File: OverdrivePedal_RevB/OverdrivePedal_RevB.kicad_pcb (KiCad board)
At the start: 2 copper layers, 26.7 x 33.7 mm, 23 parts, among them J1 Conn_01x02, J2 Conn_01x02, J3 Conn_01x03, J4 Conn_01x03, J5 Conn_01x03, J6 Conn_01x02, U1 TL072, U2 NCP1729, U3 MIC5233-5.0YM5-TR, U4 MIC5270-5.0YM5-TR

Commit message: modified RevB
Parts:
- removed U1: TL072, Package_SO:TSSOP-8_4.4x3mm_P0.65mm
- added C10: 330nF, Capacitor_SMD:C_0805_2012Metric_Pad1.15x1.40mm_HandSolder, F.Cu at (67.3, 193.7)
- added C11: 1uF, Capacitor_SMD:C_0805_2012Metric_Pad1.15x1.40mm_HandSolder, F.Cu at (78.7, 192.2)
- added U5: XC6902N501PR-G, Package_TO_SOT_SMD:SOT-89-3, F.Cu at (79.7, 196.5)
- C3: value 100nF -> 1uF
- C4, C5: value 10uF -> 1uF; footprint Capacitor_SMD:CP_Elec_4x5.7 -> Capacitor_SMD:C_0805_2012Metric_Pad1.15x1.40mm_HandSolder
- C8: value 2.2uF -> 100nF
- J1, J2, J3, J4, J5, J6: moved to B.Cu
- U2: value NCP1729 -> TL071; footprint Package_TO_SOT_SMD:SOT-23-6_Handsoldering -> Package_SO:SOIC-8_3.9x4.9mm_P1.27mm
- U3: value MIC5233-5.0YM5-TR -> TPS60400
- U4: value MIC5270-5.0YM5-TR -> KIA78L05T; footprint Package_TO_SOT_SMD:SOT-23-5_HandSoldering -> Package_TO_SOT_SMD:SOT-89-3
- moved U2 20.8 mm to (72.6, 176.0), turned to 0 degrees
- moved C4 12.7 mm to (70.6, 198.2)
- moved C8 10.7 mm to (72.4, 187.3), turned to 180 degrees
- moved C6 10.5 mm to (80.2, 200.2), turned to 180 degrees
- moved U3 10.5 mm to (74.2, 197.2), turned to 0 degrees
- moved U4 7.54 mm to (71.9, 190.9), turned to 270 degrees
- moved J5 7.40 mm to (78.2, 188.0), turned to 0 degrees
- moved C5 6.83 mm to (75.8, 193.2), turned to 90 degrees
- moved R2 5.86 mm to (62.5, 177.7)
- moved C3 5.22 mm to (73.9, 200.2)
- moved C9 5.14 mm to (70.1, 181.0), turned to 270 degrees
- moved J2 4.54 mm to (67.2, 199.3), turned to 0 degrees
- moved R1 4.34 mm to (67.4, 177.7), turned to 270 degrees
- moved J6 4.18 mm to (82.1, 185.4), turned to 0 degrees
- moved D1 3.42 mm to (63.5, 196.1), turned to 270 degrees
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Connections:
- C3 pad 1: +5V -> Net-(C3-Pad1)
- C3 pad 2: GNDS -> Net-(C3-Pad2)
- C4 pad 1: Net-(C4-Pad1) -> +5V
- C4 pad 2: Net-(C4-Pad2) -> GNDS
- C5 pad 1: GNDS -> /PosNeg5V_PSU/-5V_POL
- C5 pad 2: /PosNeg5V_PSU/-5V_POL -> GNDS
- U2 pad 1: /PosNeg5V_PSU/-5V_POL -> Net-(U2-Pad1)
- U2 pad 2: +5V -> Net-(J4-Pad2)
- U2 pad 3: Net-(C4-Pad2) -> Net-(C1-Pad1)
- U2 pad 4: GNDS -> -5V
- U2 pad 5: +5V -> Net-(U2-Pad5)
- U2 pad 6: Net-(C4-Pad1) -> Net-(C2-Pad2)
- U3 pad 1: /PosNeg5V_PSU/+9V_POL -> /PosNeg5V_PSU/-5V_POL
- U3 pad 2: GNDS -> +5V
- U3 pad 3: /PosNeg5V_PSU/+9V_POL -> Net-(C3-Pad1)
- U3 pad 4: Net-(U3-Pad4) -> GNDS
- U3 pad 5: +5V -> Net-(C3-Pad2)
- U4 pad 1: Net-(U4-Pad1) -> +5V
- U4 pad 3: Net-(U4-Pad3) -> /PosNeg5V_PSU/+9V_POL
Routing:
- net +5V: track 80.1 -> 40.6 mm
- net GNDS: track 24.8 -> 0.00 mm
- net -5V: track 30.3 -> 54.9 mm
- net Net-(J3-Pad3): track 6.60 -> 15.5 mm
- net Net-(C4-Pad1): track 7.85 -> 0.00 mm
- net Net-(U1-Pad1): track 7.09 -> 0.00 mm
- net Net-(J4-Pad2): track 16.8 -> 23.3 mm
- net Net-(C3-Pad2): track 0.00 -> 5.01 mm
- net Net-(C4-Pad2): track 4.32 -> 0.00 mm
- net /PosNeg5V_PSU/+9V_POL: track 7.85 -> 11.4 mm
- net Net-(C1-Pad1): track 7.36 -> 5.31 mm
- net Net-(C3-Pad1): track 0.00 -> 1.97 mm
- net Net-(C2-Pad2): track 9.99 -> 11.7 mm
- net /PosNeg5V_PSU/-5V_POL: track 14.8 -> 13.6 mm
- net Net-(C1-Pad2): track 4.19 -> 5.03 mm
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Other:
- board size 26.7 x 33.7 mm -> 26.7 x 34.9 mm

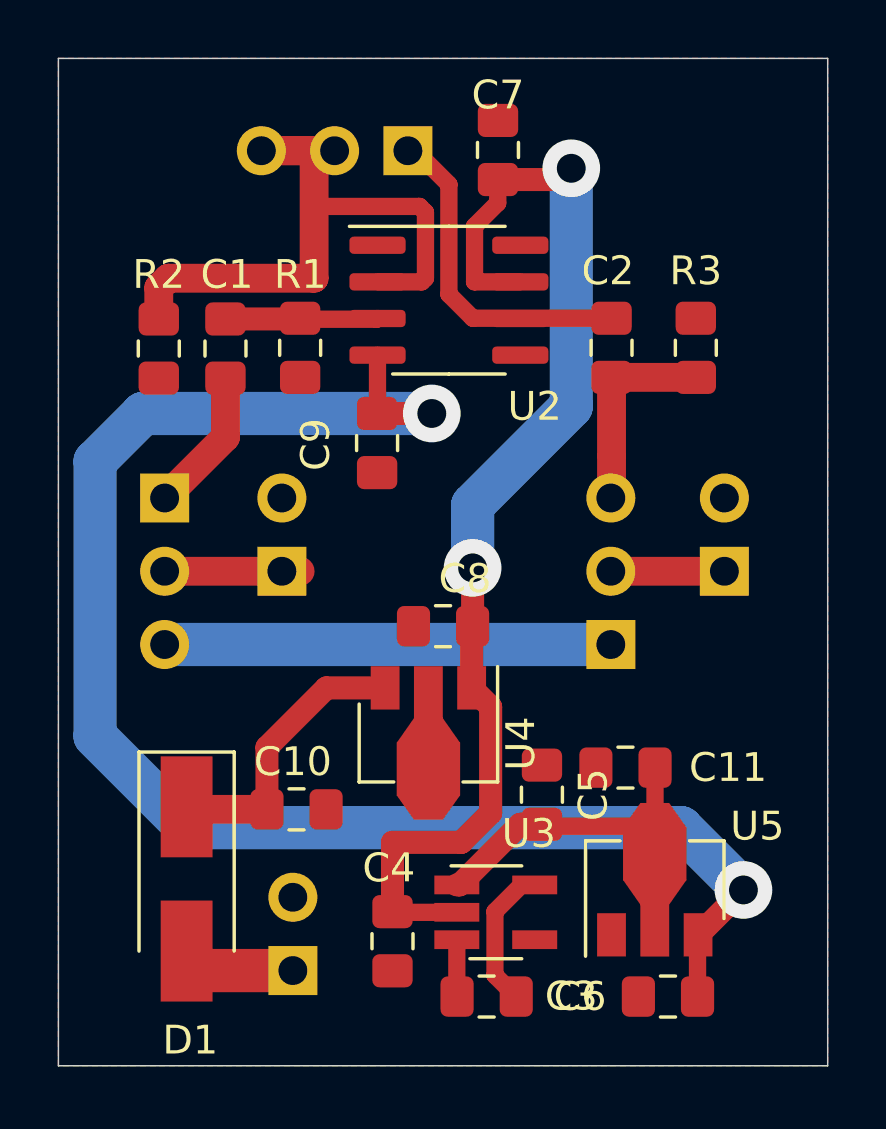
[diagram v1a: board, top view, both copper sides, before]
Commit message: Added gnd plane revb
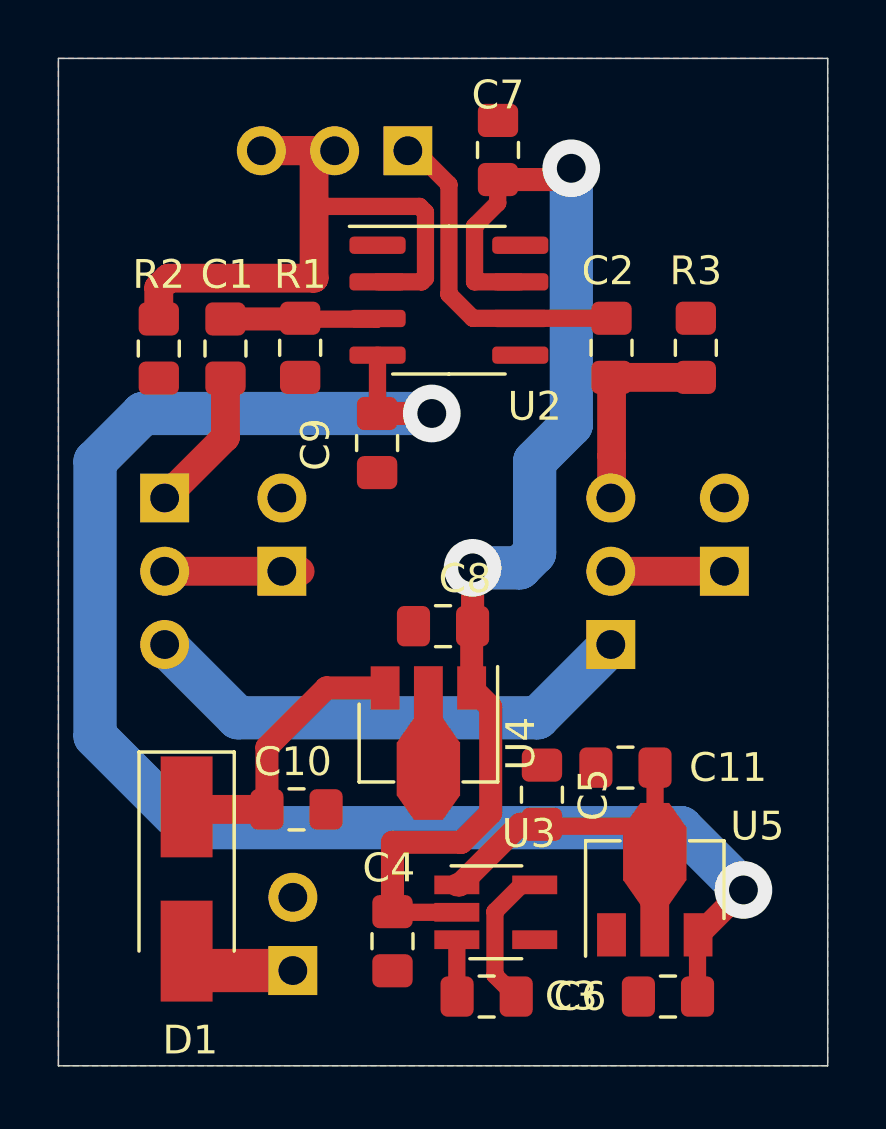
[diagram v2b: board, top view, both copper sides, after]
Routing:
- net Net-(J3-Pad3): track 15.5 -> 17.6 mm
- net +5V: track 40.6 -> 41.6 mm
- added copper zone on B.Cu, net GNDS
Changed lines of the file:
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@@
-(kicad_pcb (version 20171130) (host pcbnew 5.1.5-52549c5~84~ubuntu18.04.1)
+(kicad_pcb (version 20171130) (host pcbnew "(5.1.5-0-10_14)")
   (general
     (thickness 1.6)
     (drawings 5)
-    (tracks 92)
+    (tracks 96)
     (zones 0)
     (modules 25)
@@
   )
   (setup
-    (last_trace_width 1.5)
+    (last_trace_width 0.25)
     (user_trace_width 0.45)
     (user_trace_width 0.6)
@@
   (via (at 76.835 171.45) (size 2) (drill 1) (layers F.Cu B.Cu) (net 3))
   (segment (start 76.445 171.84) (end 76.835 171.45) (width 0.8) (layer F.Cu) (net 3))
-  (segment (start 76.835 171.45) (end 76.835 179.705) (width 1.5) (layer B.Cu) (net 3))
-  (segment (start 73.415 183.125) (end 73.415 185.302) (width 1.5) (layer B.Cu) (net 3))
-  (segment (start 76.835 179.705) (end 73.415 183.125) (width 1.5) (layer B.Cu) (net 3))
+  (segment (start 75.048 185.302) (end 73.415 185.302) (width 1.5) (layer B.Cu) (net 3))
+  (segment (start 75.565 184.785) (end 75.048 185.302) (width 1.5) (layer B.Cu) (net 3))
+  (segment (start 75.565 181.61) (end 75.565 184.785) (width 1.5) (layer B.Cu) (net 3))
+  (segment (start 76.835 180.34) (end 75.565 181.61) (width 1.5) (layer B.Cu) (net 3))
+  (segment (start 76.835 171.45) (end 76.835 180.34) (width 1.5) (layer B.Cu) (net 3))
   (segment (start 81.2128 198.0582) (end 81.1798 198.0252) (width 0.6) (layer F.Cu) (net 4))
   (segment (start 81.2128 200.1012) (end 81.2128 198.0582) (width 0.6) (layer F.Cu) (net 4))
@@
   (segment (start 63.921 199.263) (end 63.754 199.096) (width 1.5) (layer F.Cu) (net 6))
   (segment (start 67.183 199.263) (end 63.921 199.263) (width 1.5) (layer F.Cu) (net 6))
-  (segment (start 62.738 187.96) (end 78.2066 187.96) (width 1.5) (layer B.Cu) (net 7))
+  (segment (start 75.6666 190.5) (end 78.2066 187.96) (width 1.5) (layer B.Cu) (net 7))
+  (segment (start 65.278 190.5) (end 75.6666 190.5) (width 1.5) (layer B.Cu) (net 7))
+  (segment (start 62.738 187.96) (end 65.278 190.5) (width 1.5) (layer B.Cu) (net 7))
   (segment (start 68.6218 170.8314) (end 68.6308 170.8404) (width 1) (layer F.Cu) (net 8))
   (segment (start 68.6308 170.8404) (end 66.0908 170.8404) (width 1) (layer F.Cu) (net 8))
@@
     (connect_pads yes (clearance 0.508))
     (min_thickness 0.254)
+    (fill yes (arc_segments 32) (thermal_gap 0.508) (thermal_bridge_width 0.508))
+    (polygon
+      (pts
+        (xy 85.725 202.565) (xy 59.055 202.565) (xy 59.055 167.64) (xy 85.725 167.64)
+      )
+    )
+  )
+  (zone (net 1) (net_name GNDS) (layer B.Cu) (hatch edge 0.508)
+    (connect_pads yes (clearance 0.508))
+    (min_thickness 0.254)

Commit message: updated revb
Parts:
- removed C11, C6: 1uF, Capacitor_SMD:C_0805_2012Metric_Pad1.15x1.40mm_HandSolder
- removed J4: Conn_01x03, Connector_PinHeader_2.54mm:PinHeader_1x03_P2.54mm_Vertical
- removed U5: XC6902N501PR-G, Package_TO_SOT_SMD:SOT-89-3
- added D2: LED, LED_SMD:LED_1206_3216Metric_Pad1.42x1.75mm_HandSolder, B.Cu at (80.1, 198.9)
- added D3: LED, LED_SMD:LED_1206_3216Metric_Pad1.42x1.75mm_HandSolder, B.Cu at (82.0, 172.8)
- added R6: 1K, Resistor_SMD:R_0805_2012Metric_Pad1.15x1.40mm_HandSolder, B.Cu at (74.9, 198.9)
- added R9: 1K, Resistor_SMD:R_0805_2012Metric_Pad1.15x1.40mm_HandSolder, B.Cu at (82.0, 177.8)
- added RV1: B10K, Connector_PinHeader_2.54mm:PinHeader_1x03_P2.54mm_Vertical, B.Cu at (65.4, 170.8)
- D1: value D_Schottky -> BYS12-90; footprint Diode_SMD:D_SMA_Handsoldering -> Diode_SMD:D_SOD-123F
- J1, J6: value Conn_01x02 -> AudioJack2
- J2: value Conn_01x02 -> Barrel_Jack
- moved C7 6.57 mm to (79.2, 175.1), turned to 0 degrees
- moved U3 5.36 mm to (79.6, 196.7)
- moved C3 5.36 mm to (79.2, 199.7)
- moved C4 5.08 mm to (75.7, 197.7)
- moved C10 3.21 mm to (64.3, 194.7), turned to 270 degrees
- moved C1 2.72 mm to (67.6, 177.7)
- moved J2 2.63 mm to (69.8, 198.9), turned to 90 degrees
- moved C5 2.44 mm to (78.2, 192.8)
- moved R1 2.41 mm to (65.0, 177.7)
- moved D1 2.05 mm to (61.7, 195.1)
- moved C2 0.76 mm to (78.2, 178.4)
- moved R3 0.76 mm to (81.2, 178.4)
- moved J1 0.51 mm to (67.3, 185.4)
- moved J6 0.10 mm to (82.0, 185.4)
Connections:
- C5 pad 1: /PosNeg5V_PSU/-5V_POL -> -5V
- J2 pad 1: /PosNeg5V_PSU/+9V_IN -> GNDS
- J2 pad 2: GNDS -> /PosNeg5V_PSU/+9V_IN
- U3 pad 1: /PosNeg5V_PSU/-5V_POL -> -5V
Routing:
- net /PosNeg5V_PSU/-5V_POL: track 13.6 -> 0.00 mm
- net -5V: track 54.9 -> 61.3 mm
- net /PosNeg5V_PSU/+9V_IN: track 3.50 -> 7.56 mm
- net Net-(C1-Pad2): track 5.03 -> 8.39 mm
- net +5V: track 41.6 -> 44.9 mm
- net Net-(D2-Pad2): track 0.00 -> 2.54 mm
- net Net-(D3-Pad1): track 0.00 -> 2.31 mm
- net Net-(J3-Pad3): track 17.6 -> 15.5 mm
- net Net-(R2-Pad1): track 23.3 -> 21.5 mm
- net Net-(C2-Pad2): track 11.7 -> 12.6 mm
- net Net-(C2-Pad1): track 7.00 -> 6.24 mm
- net Net-(J1-Pad1): track 4.06 -> 4.57 mm
- net GNDS: vias 0 -> 1

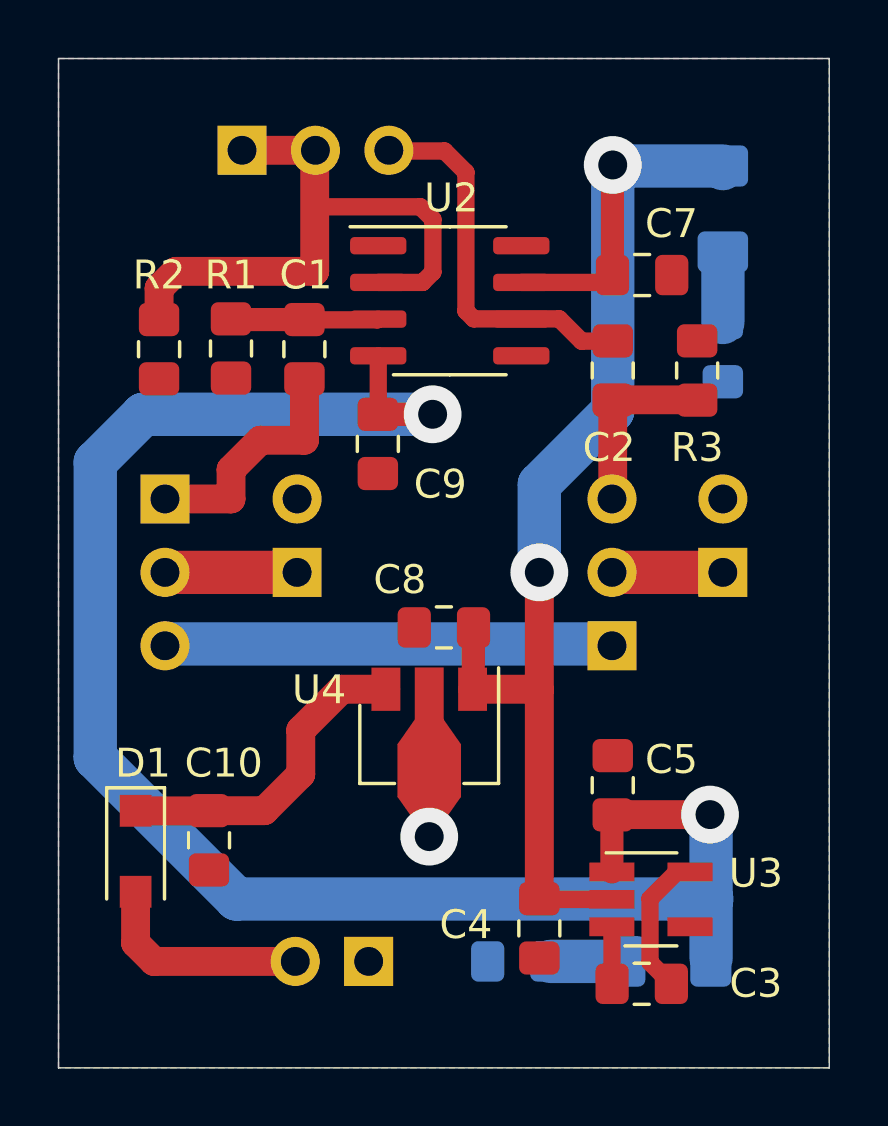
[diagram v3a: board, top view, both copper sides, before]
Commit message: Added extra leds
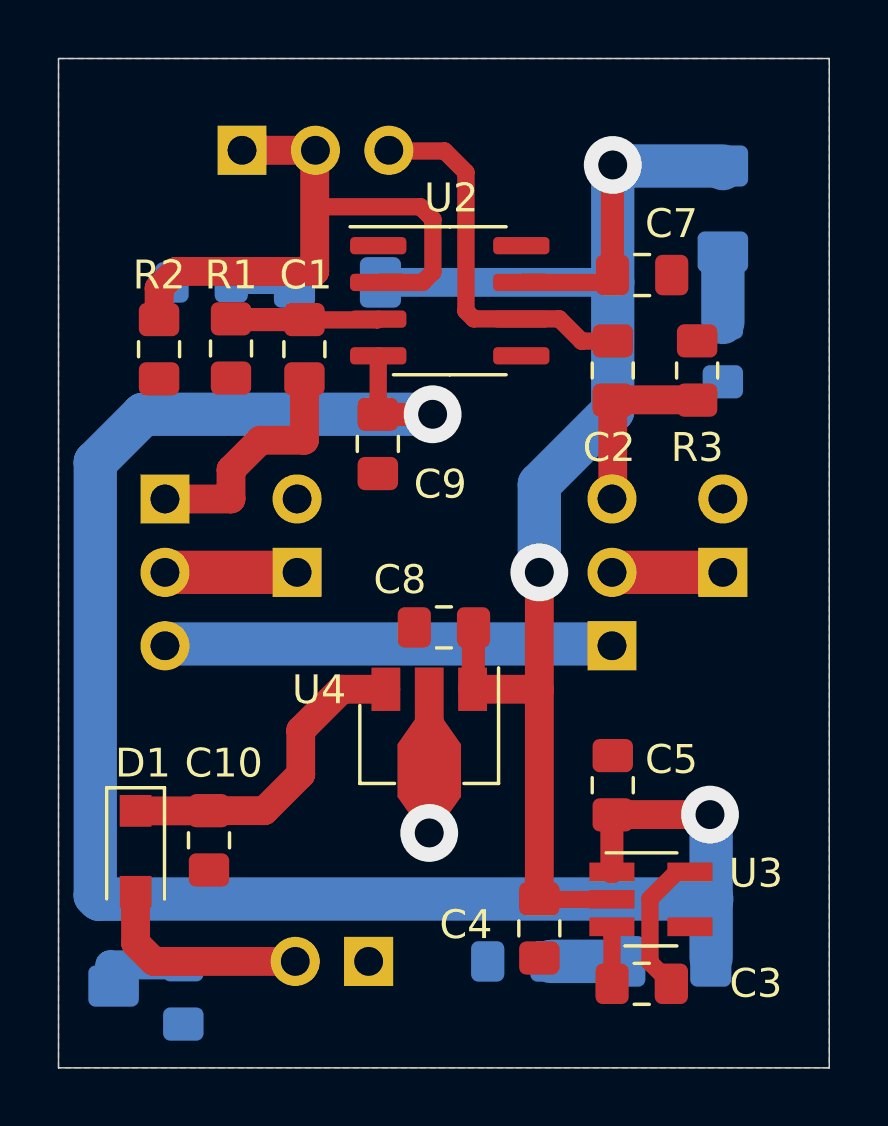
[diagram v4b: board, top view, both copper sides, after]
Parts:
- added D4: LED, LED_SMD:LED_1206_3216Metric_Pad1.42x1.75mm_HandSolder, B.Cu at (61.0, 198.2)
- added D5: LED, LED_SMD:LED_1206_3216Metric_Pad1.42x1.75mm_HandSolder, B.Cu at (68.7, 175.4)
- added R4: 1K, Resistor_SMD:R_0805_2012Metric_Pad1.15x1.40mm_HandSolder, B.Cu at (63.4, 200.0)
- added R5: 1K, Resistor_SMD:R_0805_2012Metric_Pad1.15x1.40mm_HandSolder, B.Cu at (64.0, 175.4)
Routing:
- net +5V: track 44.9 -> 52.9 mm
- net Net-(D4-Pad2): track 0.00 -> 3.24 mm
- net -5V: track 61.3 -> 64.1 mm
- net Net-(D5-Pad1): track 0.00 -> 2.19 mm
